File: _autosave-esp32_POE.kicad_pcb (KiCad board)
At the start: 2 copper layers, 204.8 x 25 mm, 68 parts, among them IC1 TPS2373-4RGWR, J1 USB_C_Receptacle_USB2.0_14P, J10 Conn_01x02, J2 WE-RJ45LAN 10/100BaseT PoE, J3 Screw_Terminal_01x03, J4 Screw_Terminal_01x03, J5 Screw_Terminal_01x03, J6 Screw_Terminal_01x03, J7 Conn_01x04, J8 Conn_01x02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

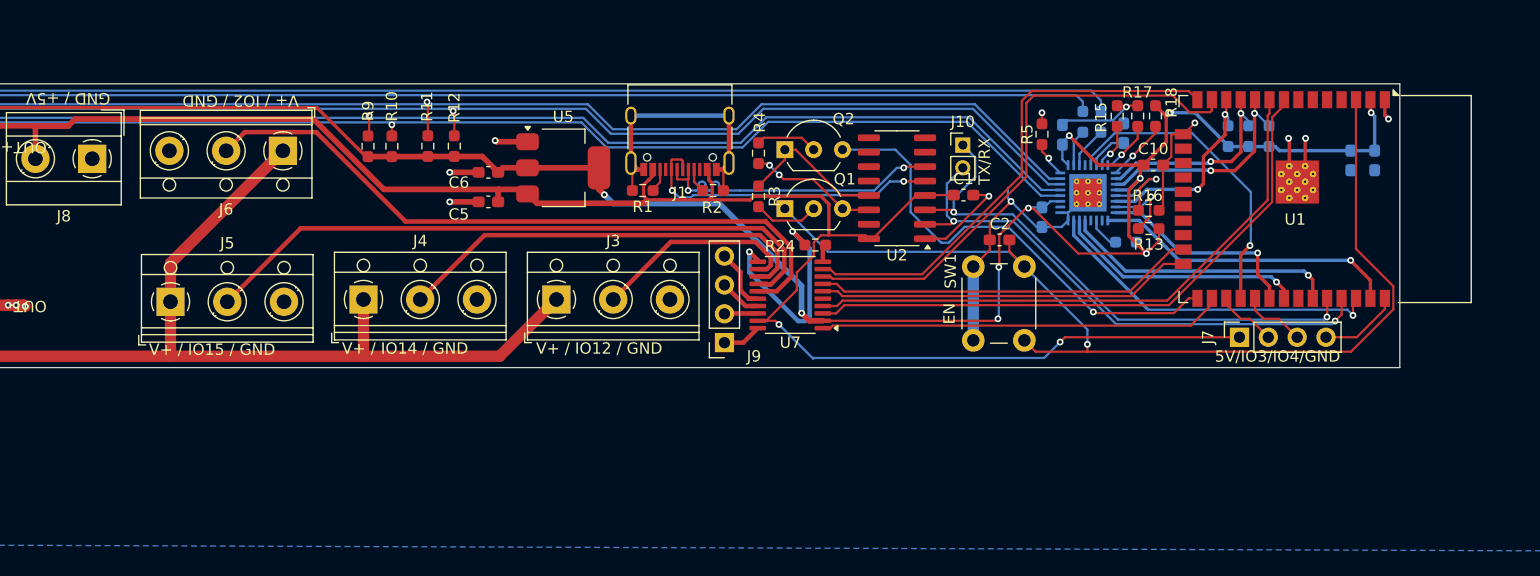
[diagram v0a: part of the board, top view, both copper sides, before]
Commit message: Modified schematic : fixed esp32 circuit, changed to SN74 level shifter, changed to LAN8270
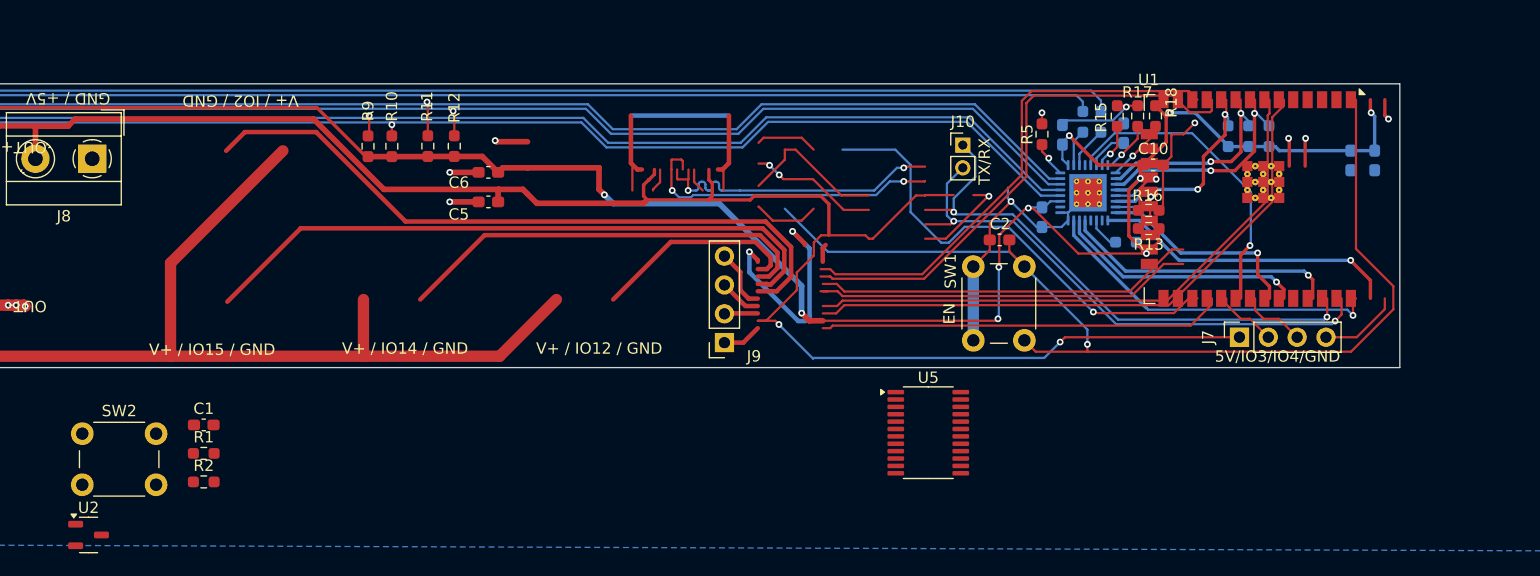
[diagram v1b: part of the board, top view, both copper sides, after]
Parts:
- removed J1: USB_C_Receptacle_USB2.0_14P, Connector_USB:USB_C_Receptacle_XKB_U262-16XN-4BVC11
- removed J3, J4, J5, J6: Screw_Terminal_01x03, TerminalBlock_RND:TerminalBlock_RND_205-00013_1x03_P5.00mm_Horizontal
- removed Q1, Q2: NPN, Package_TO_SOT_THT:TO-92_Inline_Wide
- removed R24: 12.1k, Resistor_SMD:R_0603_1608Metric_Pad0.98x0.95mm_HandSolder
- removed R3, R4: 10k, Resistor_SMD:R_0603_1608Metric_Pad0.98x0.95mm_HandSolder
- removed U7: TXS0108EPW, Package_SO:TSSOP-20_4.4x6.5mm_P0.65mm
- added SW2: SW_Push, Button_Switch_THT:SW_PUSH_6mm_H4.3mm, F.Cu at (149.6, 149.8)
- C1: value 100nF -> 2.2uF
- C5, C6: value 10uF -> 1uF
- R1, R2: value 5.1k -> 10k
- U1: footprint RF_Module:ESP32-WROOM-32D -> RF_Module:ESP32-WROOM-32E
- U2: value CH340C -> XC6206PxxxMR; footprint Package_SO:SOIC-16_3.9x9.9mm_P1.27mm -> Package_TO_SOT_SMD:SOT-23-3
- U5: value AMS1117-3.3 -> SN74LVC8T245; footprint Package_TO_SOT_SMD:SOT-223-3_TabPin2 -> Package_SO:TSSOP-24_4.4x7.8mm_P0.65mm
- moved U2 77.5 mm to (150.2, 158.7), turned to 0 degrees
- moved C1 69.9 mm to (160.3, 149.1)
- moved R2 51.7 mm to (160.3, 154.1)
- moved R1 45.1 mm to (160.3, 151.6), turned to 0 degrees
- moved U5 39.7 mm to (224.2, 149.7)
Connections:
- C1 pad 1: +5V -> IO0
- R1 pad 1: Net-(J1-CC2) -> +3.3V
- R1 pad 2: GND -> IO0
- R2 pad 1: Net-(J1-CC1) -> +3.3V
- R2 pad 2: GND -> EN
- U2 pad 2: TX -> +3.3V
- U2 pad 3: RX -> +5V
- U5 pad 1: GND -> +5V
- U5 pad 2: +3.3V -> GND
- U5 pad 3: +5V -> Net-(J9-Pin_1)
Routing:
- net (no net): track 0.00 -> 97.0 mm, vias 0 -> 6
- net Net-(J6-Pin_2): track 60.7 -> 0.00 mm
- net CLK: track 27.6 -> 63.2 mm
- net BRKOUT4: track 35.7 -> 0.00 mm
- net CHANNEL2: track 33.6 -> 0.00 mm
- net CHANNEL1: track 33.8 -> 67.3 mm
- net D+: track 27.6 -> 0.00 mm, vias 2 -> 0
- net D-: track 27.6 -> 0.00 mm, vias 2 -> 0
- net Net-(J4-Pin_2): track 37.9 -> 57.2 mm
- net Net-(J3-Pin_2): track 18.5 -> 37.9 mm
- net Net-(J1-Pin_2): track 0.00 -> 18.5 mm
- net Net-(Q2-C): track 13.2 -> 0.00 mm
- net Net-(Q1-E): track 11.4 -> 0.00 mm, vias 2 -> 0
- net Net-(Q1-B): track 5.80 -> 0.00 mm
- net Net-(Q2-B): track 5.48 -> 0.00 mm
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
